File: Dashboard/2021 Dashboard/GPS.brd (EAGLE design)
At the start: 100 x 80 mm, 1 part

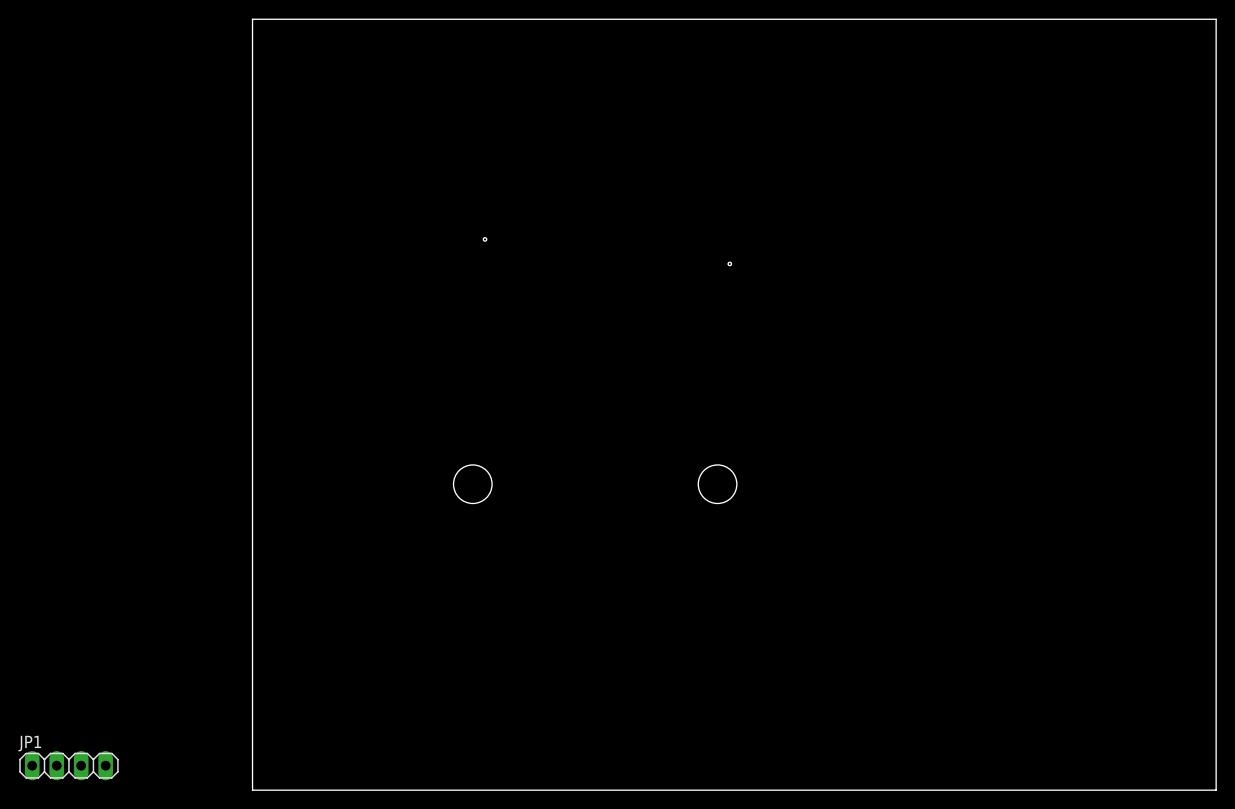
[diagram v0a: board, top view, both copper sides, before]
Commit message: More work done to dash hub and dial, gps board added
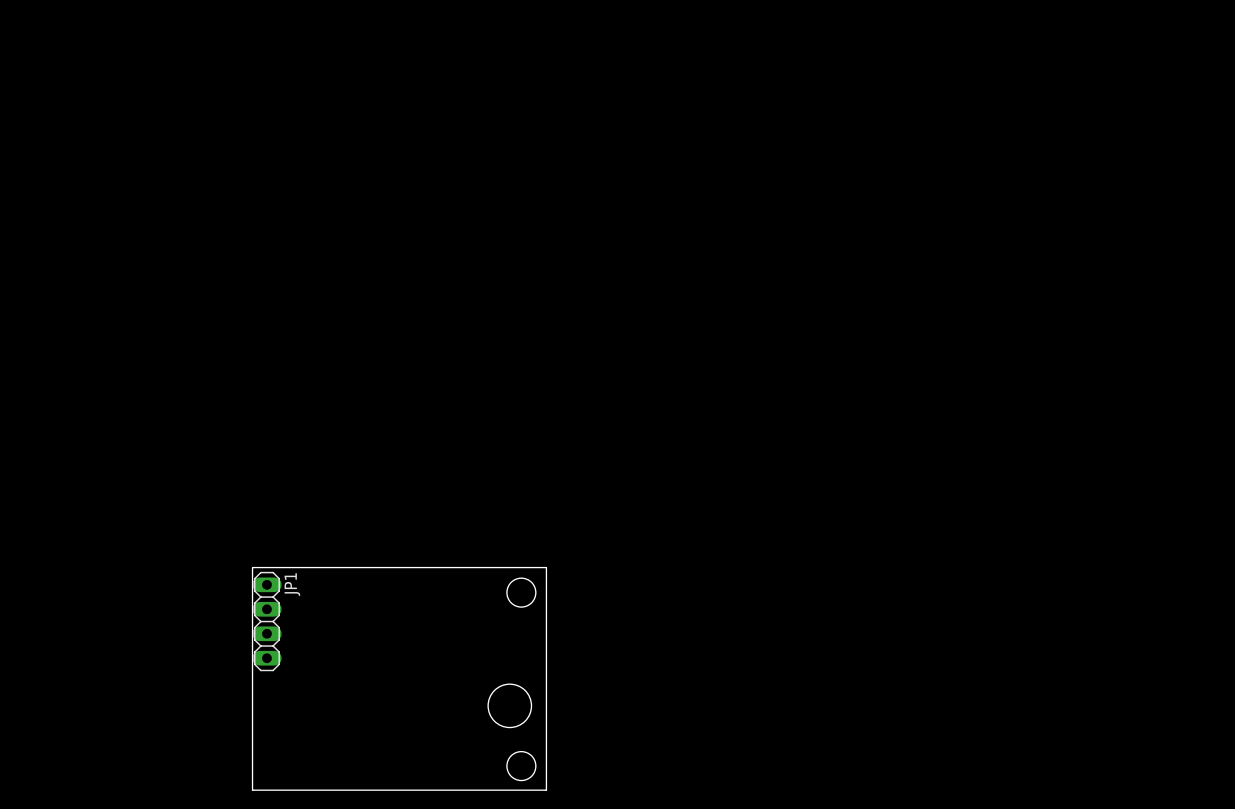
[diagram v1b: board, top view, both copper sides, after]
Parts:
- moved JP1 25.4 mm to (1.50, 17.5), turned to 270 degrees
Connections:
- net RX: now also JP1.2; no longer JP1.3
- net TX: now also JP1.3; no longer JP1.2
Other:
- board size 100 x 80 mm -> 30.5 x 23.1 mm
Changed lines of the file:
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@@
 <setting verticaltext="up"/>
 </settings>
-<grid distance="50" unitdist="mil" unit="mil" style="lines" multiple="1" display="no" altdistance="5" altunitdist="mil" altunit="mil"/>
+<grid distance="1" unitdist="mm" unit="mm" style="lines" multiple="1" display="no" altdistance="5" altunitdist="mil" altunit="mm"/>
 <layers>
 <layer number="1" name="Top" color="4" fill="1" visible="yes" active="yes"/>
@@
 <board>
 <plain>
-<wire x1="0" y1="0" x2="100" y2="0" width="0" layer="20"/>
-<wire x1="100" y1="0" x2="100" y2="80" width="0" layer="20"/>
-<wire x1="100" y1="80" x2="0" y2="80" width="0" layer="20"/>
-<wire x1="0" y1="80" x2="0" y2="0" width="0" layer="20"/>
-<hole x="24.13" y="57.15" drill="0.35"/>
-<hole x="22.86" y="31.75" drill="4"/>
-<hole x="48.26" y="31.75" drill="4"/>
-<hole x="49.53" y="54.61" drill="0.35"/>
+<wire x1="0" y1="0" x2="30.5" y2="0" width="0" layer="20"/>
+<wire x1="30.5" y1="0" x2="30.5" y2="23.1" width="0" layer="20"/>
+<wire x1="30.5" y1="23.1" x2="0" y2="23.1" width="0" layer="20"/>
+<wire x1="0" y1="23.1" x2="0" y2="0" width="0" layer="20"/>
+<hole x="27.9" y="20.5" drill="3"/>
+<hole x="27.9" y="2.5" drill="3"/>
+<hole x="26.7" y="8.75" drill="4.5"/>
 </plain>
 <attributes>
@@
 </autorouter>
 <elements>
-<element name="JP1" library="GTOR - Connectors" package="1X04" package3d_urn="urn:adsk.eagle:package:22407/2" value="" x="-19.05" y="2.54" smashed="yes">
-<attribute name="NAME" x="-24.2062" y="4.3688" size="1.27" layer="25" ratio="10"/>
-<attribute name="POPULARITY" value="91" x="0" y="0" size="1.778" layer="27" display="off"/>
-<attribute name="VALUE" x="-24.13" y="-0.635" size="1.27" layer="27"/>
+<element name="JP1" library="GTOR - Connectors" package="1X04" package3d_urn="urn:adsk.eagle:package:22407/2" value="" x="1.5" y="17.5" smashed="yes" rot="R270">
+<attribute name="NAME" x="3.3288" y="22.6562" size="1.27" layer="25" ratio="10" rot="R270"/>
+<attribute name="POPULARITY" value="91" x="-1.04" y="-1.55" size="1.778" layer="27" rot="R270" display="off"/>
+<attribute name="VALUE" x="-1.675" y="22.58" size="1.27" layer="27" rot="R270"/>
 </element>
 </elements>
 <signals>
-<signal name="RX">
-<contactref element="JP1" pad="3"/>
-</signal>
-<signal name="TX">
-<contactref element="JP1" pad="2"/>
-</signal>
 <signal name="GND">
 <contactref element="JP1" pad="1"/>
@@
 <signal name="+3V3">
 <contactref element="JP1" pad="4"/>
+</signal>
+<signal name="TX">
+<contactref element="JP1" pad="3"/>
+</signal>
+<signal name="RX">
+<contactref element="JP1" pad="2"/>
 </signal>
 </signals>
@@
 <mfgpreviewcolor name="substratecolor" color="0xFF786E46"/>
 </mfgpreviewcolors>
+<errors>
+</errors>
 </board>
 </drawing>
